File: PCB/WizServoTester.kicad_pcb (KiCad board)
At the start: 2 copper layers, 100 x 60.5 mm, 42 parts, among them J1 USB_C_Receptacle_USB2.0_16P, J2 Servo_3_Header, J3 Servo_4_Header, J4 Servo_1_Header, J5 Servo_2_Header, J6 BAT_XT30, J8 BAT_Pads, SW1 EC 11, SW2 EC 11, SW3 EC 11, SW4 EC 11, SW5 SW_Push, SW6 SW_SPDT, SW7 SW_Push, U1 ESP32-C6-WROOM-1, U2 USBLC6-2SC6, U3 AMS1117-3.3, U4 Mini560

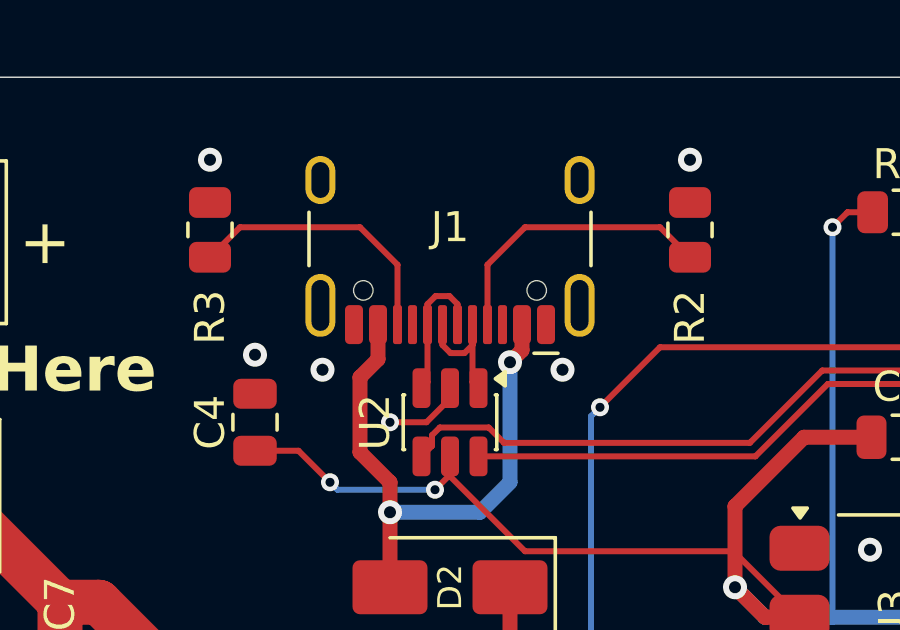
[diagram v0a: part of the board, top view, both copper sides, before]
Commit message: Added Case and Production Files
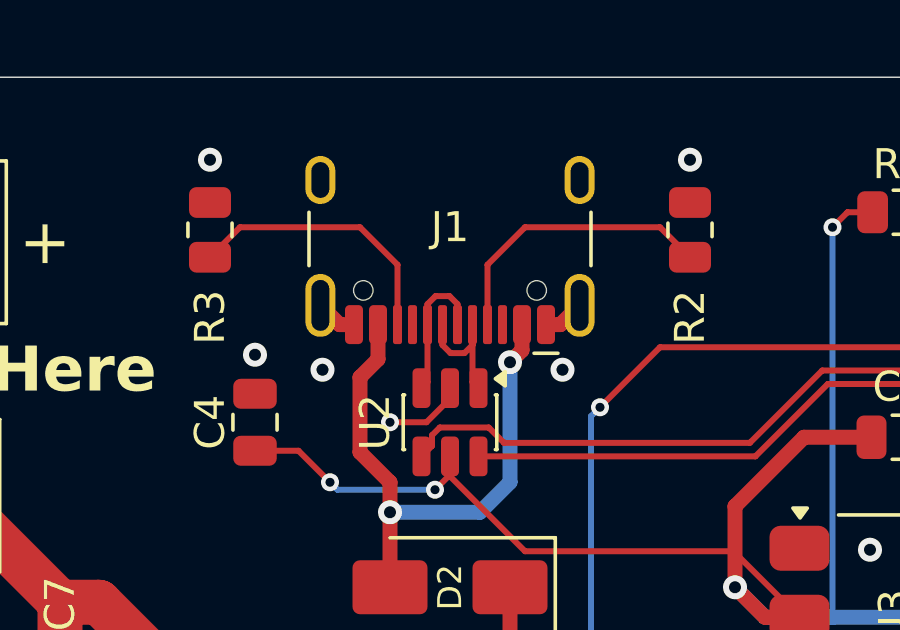
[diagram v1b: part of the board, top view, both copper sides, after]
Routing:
- net GND: track 2.68 -> 5.45 mm

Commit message: Pcb fixes
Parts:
- removed D1, D3: ESD9B3.3, Diode_SMD:D_SOD-923
- turned C8 to -45 degrees
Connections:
- C8 pad 1: +5V -> BAT5v
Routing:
- net +5V: track 197.2 -> 104.1 mm
- net BAT5v: track 18.2 -> 66.7 mm
- net Boot: track 37.1 -> 29.7 mm
- net EN: track 68.7 -> 62.3 mm
